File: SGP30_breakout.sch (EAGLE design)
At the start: 12 parts, among them IC1 MCP1703T-1802E/CB, Q1 220mA/50V/3.5Ω, Q2 220mA/50V/3.5Ω

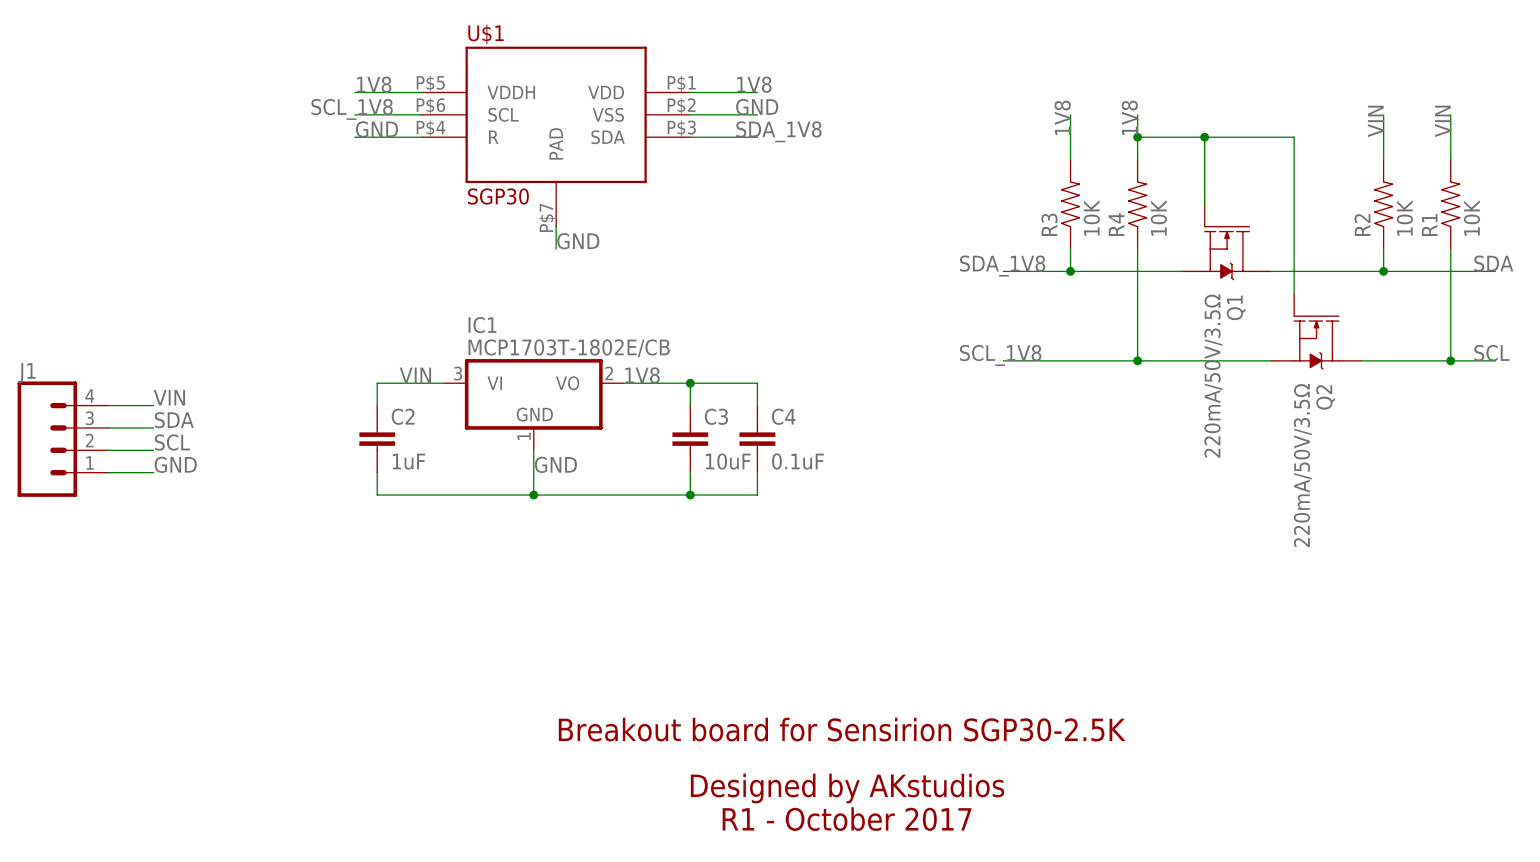
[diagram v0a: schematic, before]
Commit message: R2 - bug fixes
- GND and SCL trace swapped
- shrinked board size
- silkscreen adjustments
- removed GND plane
- routed GND trace
- trace adjustments
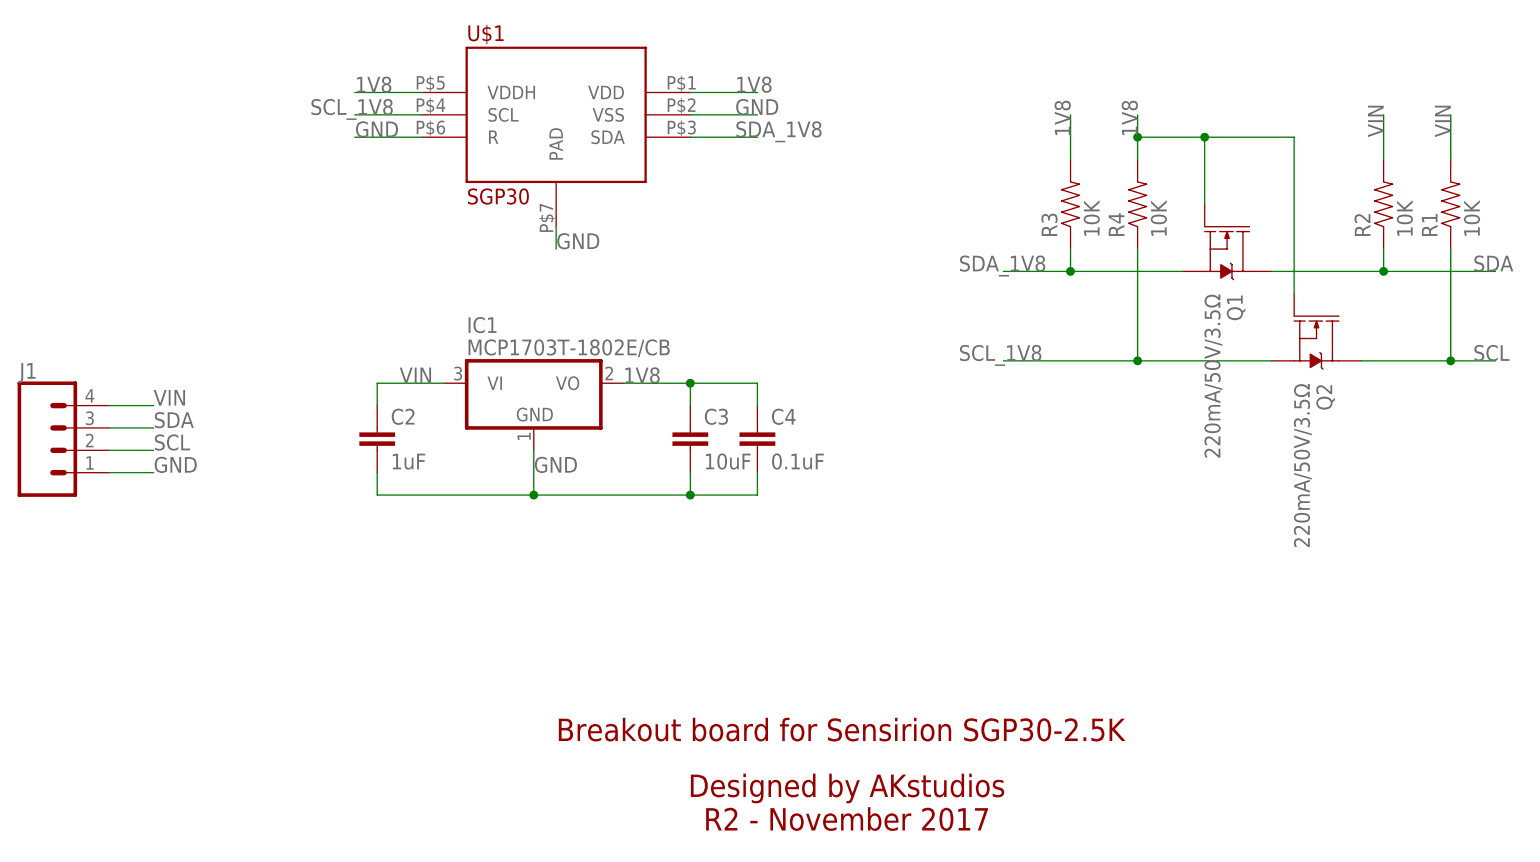
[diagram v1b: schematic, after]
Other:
- note added: "Designed by AKstudios R2 - November 2017"
- note removed: "Designed by AKstudios R1 - October 2017"
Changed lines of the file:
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@@
 <text x="60.96" y="-25.4" size="2.54" layer="94" font="vector">Breakout board for Sensirion SGP30-2.5K</text>
 <text x="93.98" y="-35.56" size="2.54" layer="94" font="vector" align="bottom-center">Designed by AKstudios
-R1 - October 2017</text>
+R2 - November 2017</text>
 </plain>
 <instances>
